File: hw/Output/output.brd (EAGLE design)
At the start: 60.6 x 71.1 mm, 20 parts, among them Q1 MOSFET-NCHANNELFDD8780, Q2 MOSFET-NCHANNELFDD8780, U3 TMP102

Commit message: Added power indication LED and Battery current/voltage measurement to output board. Added atmega32u2, IMU header, Temp sensor connector, and wiz55io header to control board.
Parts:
- added C5, C6, C7: 0.1uF, SparkFun-Capacitors:0603-CAP
- added LED1: (no value), SparkFun-LED:LED-0603
- added R3: .1/1%, SparkFun-Passives:R2512
- added R6: (no value), SparkFun-Passives:0603-RES
- added U$6: INA219, INA219:SOT23-8
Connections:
- new net N$1: LED1.A, R6.1
- new net V_BATT_IN: R3.1, U$6.1, X1.21
- net GND: now also C5.2, C6.2, C7.2, LED1.C, U$6.3, U$6.7, U$6.8
- net SCL: now also U$6.5
- net SDA: now also U$6.6
- net VCC: now also C5.1, C6.1, U$6.4
- net V_BATT: now also C7.1, R3.2, R6.2, U$6.2; no longer X1.21
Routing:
- net SDA: track 54.0 -> 99.5 mm, vias 4 -> 7
- net V_BATT_IN: track 0.00 -> 39.3 mm, vias 0 -> 1
- net SCL: track 52.8 -> 89.7 mm, vias 5 -> 7
- net VCC: track 117.7 -> 149.4 mm, vias 6 -> 8
- net V_BATT: track 143.1 -> 120.4 mm, vias 3 -> 2
- net N$1: track 0.00 -> 2.13 mm
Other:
- board text added: "12V"

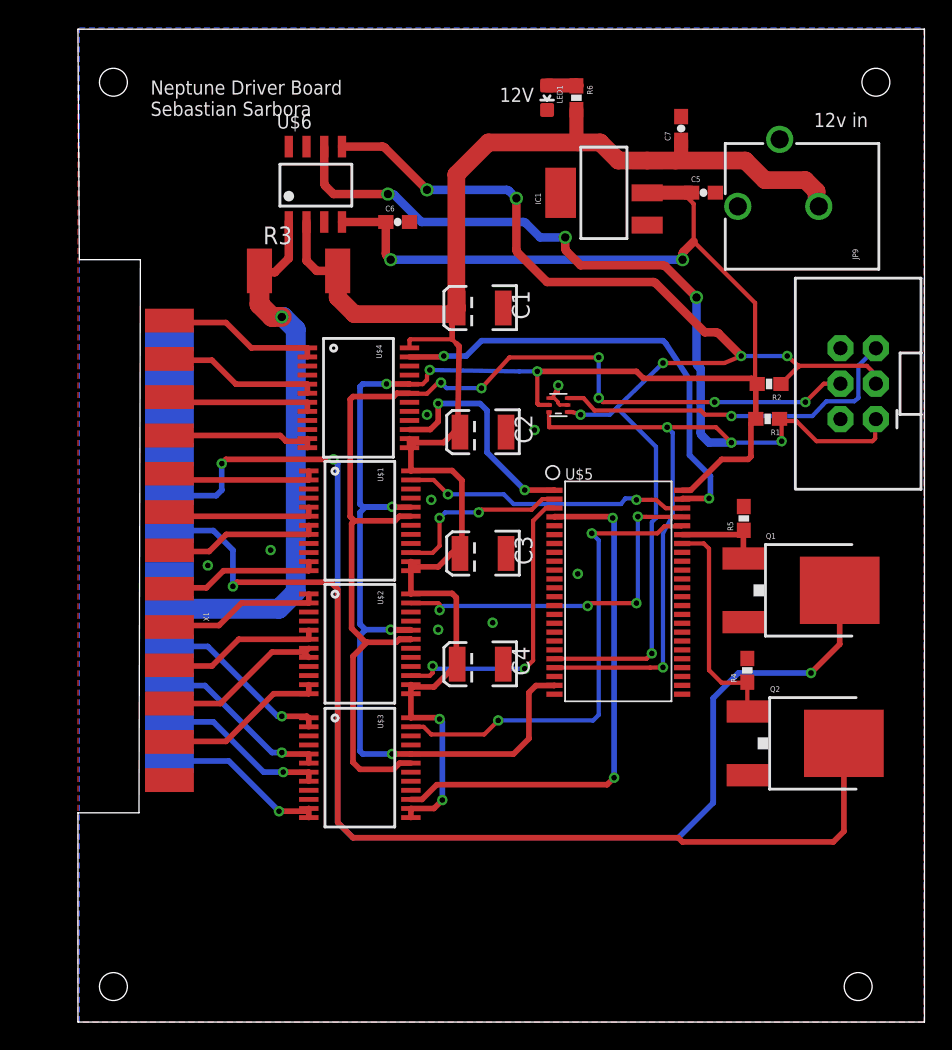
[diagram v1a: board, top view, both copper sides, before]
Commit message: Added Power Switch to output board.
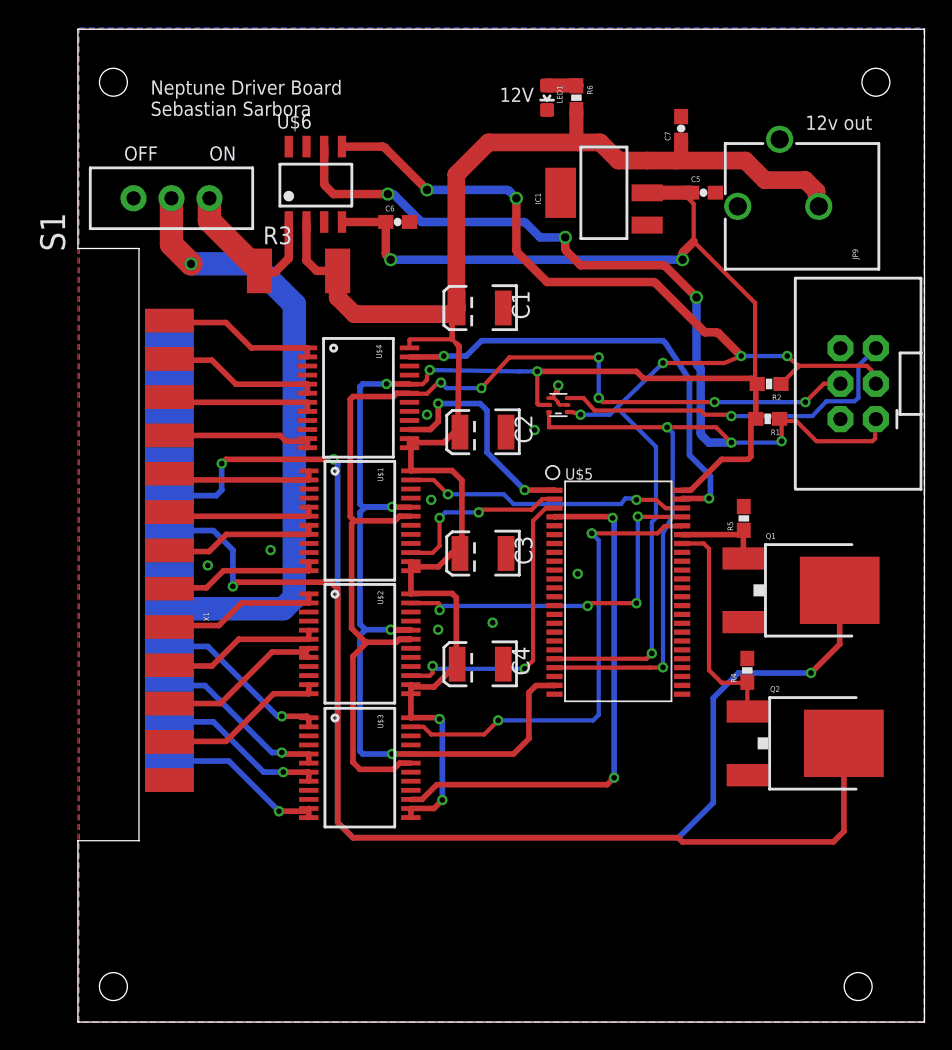
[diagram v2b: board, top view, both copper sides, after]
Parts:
- added S1: (no value), SparkFun-Electromechanical:SWITCH-SPDT_KIT
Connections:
- new net BATT: S1.2, X1.21
- net V_BATT_IN: now also S1.3; no longer X1.21
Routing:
- net BATT: track 0.00 -> 44.2 mm, vias 0 -> 1
- net V_BATT_IN: track 39.3 -> 11.8 mm, vias 1 -> 0
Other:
- outline, holes or cut-outs redrawn
- board text added: "12v out"
- board text added: "OFF"
- board text added: "ON"
- board text removed: "12v in"
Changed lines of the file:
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@@
 <wire x1="60.63" y1="0" x2="60.63" y2="71.11" width="0" layer="20"/>
 <wire x1="60.63" y1="71.11" x2="0" y2="71.11" width="0" layer="20"/>
-<wire x1="0" y1="71.11" x2="0.1" y2="54.6018" width="0" layer="20"/>
+<wire x1="0" y1="71.11" x2="0" y2="55.4018" width="0" layer="20"/>
 <hole x="55.88" y="2.54" drill="2"/>
 <hole x="57.15" y="67.31" drill="2"/>
 <hole x="2.54" y="67.31" drill="2"/>
-<wire x1="0" y1="14.986" x2="4.372" y2="14.986" width="0" layer="20"/>
-<wire x1="4.372" y1="14.986" x2="4.472" y2="54.6018" width="0" layer="20"/>
-<wire x1="4.472" y1="54.6018" x2="0.1" y2="54.6018" width="0" layer="20"/>
+<wire x1="0" y1="12.986" x2="4.372" y2="12.986" width="0" layer="20"/>
+<wire x1="4.372" y1="12.986" x2="4.372" y2="55.4018" width="0" layer="20"/>
+<wire x1="4.372" y1="55.4018" x2="0" y2="55.4018" width="0" layer="20"/>
 <hole x="2.54" y="2.54" drill="2"/>
-<wire x1="0" y1="0" x2="0" y2="14.986" width="0" layer="20"/>
+<wire x1="0" y1="0" x2="0" y2="12.986" width="0" layer="20"/>
 <text x="5.2" y="64.9" size="1.016" layer="21">Neptune Driver Board
 Sebastian Sarbora
 </text>
-<text x="52.7" y="64.1" size="1.016" layer="21">12v in</text>
 <text x="52.9" y="3.8" size="1.778" layer="22" rot="MR0">Neptune Driver Board v1.0
 Sebastian Sarbora</text>
@@
 Sebastian Sarbora</text>
 <text x="30.2" y="65.9" size="1.016" layer="21">12V</text>
+<text x="52.1" y="63.9" size="1.016" layer="21">12v out</text>
+<text x="9.4" y="61.7" size="1.016" layer="21">ON</text>
+<text x="3.3" y="61.7" size="1.016" layer="21">OFF</text>
 </plain>
 <attributes>
@@
 <element name="R6" library="SparkFun-Passives" package="0603-RES" value="" x="35.7" y="66.2" rot="R270"/>
 <element name="LED1" library="SparkFun-LED" package="LED-0603" value="" x="33.6" y="66.2" rot="R180"/>
+<element name="S1" library="SparkFun-Electromechanical" package="SWITCH-SPDT_KIT" value="" x="6.7" y="59" rot="R90">
+<attribute name="PARTNO" value="EG1218" x="6.7" y="59" size="1.016" layer="27" rot="R90" display="off"/>
+<attribute name="PROD_ID" value="SWCH-08261" x="6.7" y="59" size="1.016" layer="27" rot="R90" display="off"/>
+</element>
 </elements>
 <signals>
@@
 <signal name="V_BATT_IN">
 <contactref element="U$6" pad="1"/>
-<contactref element="X1" pad="21"/>
 <contactref element="R3" pad="1"/>
 <wire x1="15.1" y1="57.3" x2="15.1" y2="54.7" width="0.6096" layer="1"/>
@@
 <wire x1="14.1" y1="53.7" x2="13.1" y2="53.7" width="0.6096" layer="1"/>
 <wire x1="13.1" y1="53.7" x2="13" y2="53.8" width="0.6096" layer="1"/>
-<wire x1="13" y1="53.8" x2="13" y2="51.4" width="1.4224" layer="1"/>
-<wire x1="13" y1="51.4" x2="13.9" y2="50.5" width="1.4224" layer="1"/>
-<wire x1="13.9" y1="50.5" x2="14.6" y2="50.5" width="1.4224" layer="1"/>
-<via x="14.6" y="50.5" extent="1-16" drill="0.6"/>
-<wire x1="14.6" y1="50.5" x2="14.7" y2="50.5" width="1.4224" layer="16"/>
-<wire x1="14.7" y1="50.5" x2="15.6" y2="49.6" width="1.4224" layer="16"/>
-<wire x1="15.6" y1="49.6" x2="15.6" y2="30.8" width="1.4224" layer="16"/>
-<wire x1="15.6" y1="30.8" x2="14.4" y2="29.6" width="1.4224" layer="16"/>
-<wire x1="14.4" y1="29.6" x2="6.6204" y2="29.6" width="1.4224" layer="16"/>
-<wire x1="6.6204" y1="29.6" x2="6.5532" y2="29.6672" width="1.4224" layer="16"/>
+<contactref element="S1" pad="3"/>
+<wire x1="9.4178" y1="59" x2="9.4178" y2="57.3822" width="1.6764" layer="1"/>
+<wire x1="9.4178" y1="57.3822" x2="13" y2="53.8" width="1.6764" layer="1"/>
 </signal>
 <signal name="N$1">
@@
 <wire x1="35.7" y1="67.077" x2="35.7" y2="67.05" width="1.016" layer="1"/>
 </signal>
+<signal name="BATT">
+<contactref element="S1" pad="2"/>
+<contactref element="X1" pad="21"/>
+<wire x1="6.7" y1="59" x2="6.7" y2="55.7" width="1.6764" layer="1"/>
+<wire x1="6.7" y1="55.7" x2="8.1" y2="54.3" width="1.6764" layer="1"/>
+<via x="8.1" y="54.3" extent="1-16" drill="0.6"/>
+<wire x1="8.1" y1="54.3" x2="12.6" y2="54.3" width="1.6764" layer="16"/>
+<wire x1="12.6" y1="54.3" x2="15.5" y2="51.4" width="1.6764" layer="16"/>
+<wire x1="15.5" y1="51.4" x2="15.5" y2="30.4" width="1.6764" layer="16"/>
+<wire x1="15.5" y1="30.4" x2="14.7" y2="29.6" width="1.6764" layer="16"/>
+<wire x1="14.7" y1="29.6" x2="6.6204" y2="29.6" width="1.6764" layer="16"/>
+<wire x1="6.6204" y1="29.6" x2="6.5532" y2="29.6672" width="1.6764" layer="16"/>
+</signal>
 </signals>
